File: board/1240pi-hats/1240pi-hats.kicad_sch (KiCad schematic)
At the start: 0 parts

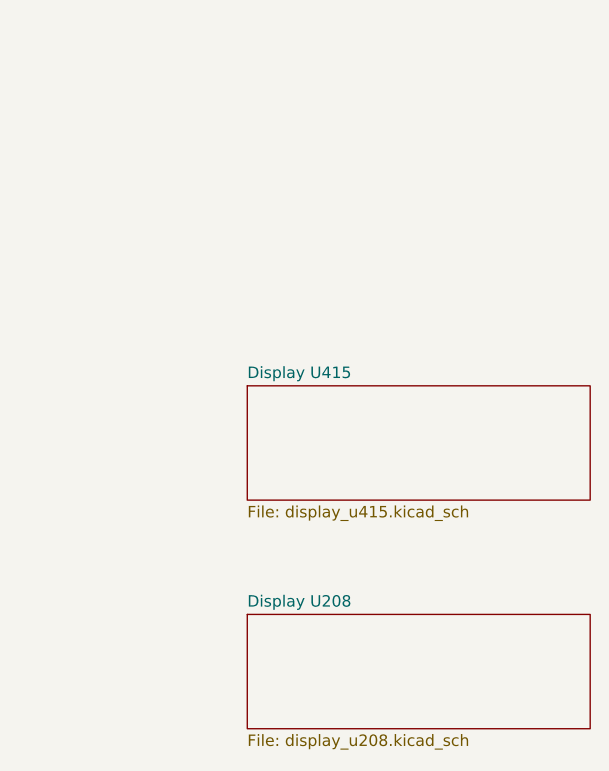
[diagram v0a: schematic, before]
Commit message: Redesign display hat to use a single board.
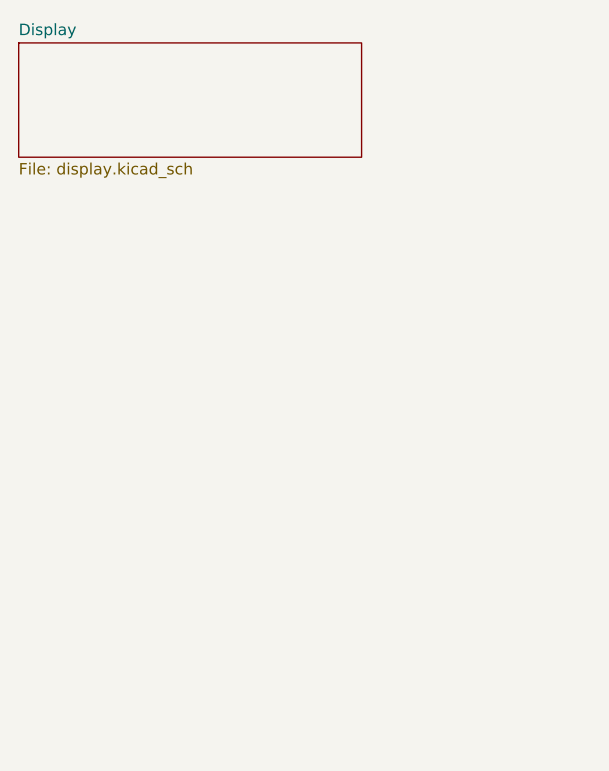
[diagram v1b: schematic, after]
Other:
- removed sheet Display U208
- removed sheet Display U415
- added sheet Display (display.kicad_sch)
- title: (none) -> 1240-Pi Mod Hats

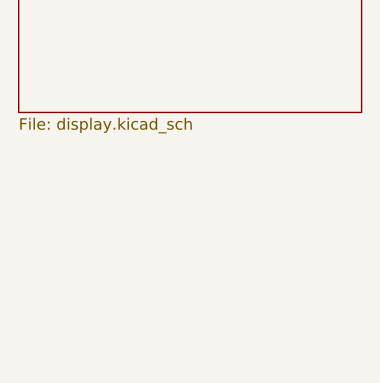
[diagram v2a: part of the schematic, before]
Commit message: Add IO Processor hat board.
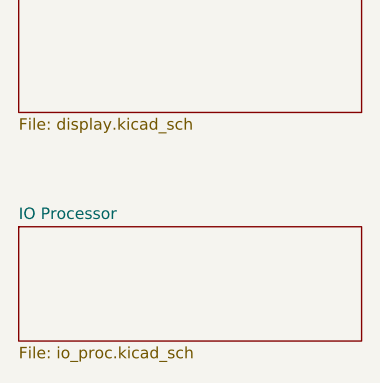
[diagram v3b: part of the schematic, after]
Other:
- added sheet IO Processor (io_proc.kicad_sch)
- company: (none) -> © 2022 Sam Hanes, licensed under CERN-OHL-P v2
- title: 1240-Pi Mod Hats -> 1240-Pi Modification Boards
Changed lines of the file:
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@@
   (paper "USLetter")
   (title_block
-    (title "1240-Pi Mod Hats")
-    (date "2022-04-20")
+    (title "1240-Pi Modification Boards")
+    (date "2022-04-21")
     (rev "1.0")
+    (company "© 2022 Sam Hanes, licensed under CERN-OHL-P v2")
+    (comment 1 "https://github.com/Elemecca/1240pi")
   )
   (sheet (at 38.1 38.1) (size 38.1 12.7) (fields_autoplaced)
@@
     )
   )
+  (sheet (at 38.1 63.5) (size 38.1 12.7) (fields_autoplaced)
+    (stroke (width 0.1524) (type solid) (color 0 0 0 0))
+    (fill (color 0 0 0 0.0000))
+    (property "Sheet name" "IO Processor" (id 0) (at 38.1 62.7884 0)
+      (effects (font (size 1.27 1.27)) (justify left bottom))
+    )
+    (property "Sheet file" "io_proc.kicad_sch" (id 1) (at 38.1 76.7846 0)
+      (effects (font (size 1.27 1.27)) (justify left top))
+    )
+  )
   (sheet_instances
     (path "/" (page "1"))
     (path "/600cca17-1832-4150-bdc4-60308bd69c4d" (page "2"))
+    (path "/93c3fd30-89aa-4f2c-a472-3cf6e18bbdfb" (page "3"))
   )
   (symbol_instances
@@
     (path "/600cca17-1832-4150-bdc4-60308bd69c4d/3702cd3c-879c-4c20-9276-eeaab458842a"
       (reference "#FLG0102") (unit 1) (value "PWR_FLAG") (footprint "")
+    )
+    (path "/93c3fd30-89aa-4f2c-a472-3cf6e18bbdfb/541631f1-5c6b-4984-b80b-da5d814ddc2a"
+      (reference "#FLG0103") (unit 1) (value "PWR_FLAG") (footprint "")
+    )
+    (path "/93c3fd30-89aa-4f2c-a472-3cf6e18bbdfb/b59ec72b-cbb3-4a84-b409-cb1a12e8909e"
+      (reference "#FLG0104") (unit 1) (value "PWR_FLAG") (footprint "")
     )
     (path "/600cca17-1832-4150-bdc4-60308bd69c4d/33dc1d17-3c43-484e-a994-57309880e165"
@@
     )
     (path "/600cca17-1832-4150-bdc4-60308bd69c4d/80a0843d-8e1d-4eab-9068-32674a47fe97"
-      (reference "#PWR?") (unit 1) (value "GND") (footprint "")
+      (reference "#PWR0105") (unit 1) (value "GND") (footprint "")
+    )
+    (path "/93c3fd30-89aa-4f2c-a472-3cf6e18bbdfb/34c1fa01-b507-49e3-9b9f-c468b6e77596"
+      (reference "#PWR0106") (unit 1) (value "~") (footprint "")
+    )
+    (path "/93c3fd30-89aa-4f2c-a472-3cf6e18bbdfb/534827d0-458c-4104-bc6d-0255ad697b4c"
+      (reference "#PWR0107") (unit 1) (value "+5V") (footprint "")
+    )
+    (path "/93c3fd30-89aa-4f2c-a472-3cf6e18bbdfb/805d731d-4180-4b8e-bf12-b88ccec030b8"
+      (reference "#PWR0108") (unit 1) (value "+5V") (footprint "")
+    )
+    (path "/93c3fd30-89aa-4f2c-a472-3cf6e18bbdfb/57c4d56d-de84-4172-ae0f-4c05a32da8d4"
+      (reference "#PWR0109") (unit 1) (value "GND") (footprint "")
+    )
+    (path "/93c3fd30-89aa-4f2c-a472-3cf6e18bbdfb/53181a90-a010-4b72-99ae-37b5bd3dc882"
+      (reference "#PWR0110") (unit 1) (value "+5V") (footprint "")
+    )
+    (path "/93c3fd30-89aa-4f2c-a472-3cf6e18bbdfb/2aecf130-835d-43a0-a6c9-612e14e7a782"
+      (reference "#PWR0111") (unit 1) (value "GND") (footprint "")
     )
     (path "/600cca17-1832-4150-bdc4-60308bd69c4d/75a11c0c-9043-4723-93bf-97178f7d2b90"
       (reference "J1") (unit 1) (value "Conn_02x05_Odd_Even") (footprint "Connector_PinHeader_2.54mm:PinHeader_2x05_P2.54mm_Vertical")
+    )
+    (path "/93c3fd30-89aa-4f2c-a472-3cf6e18bbdfb/f05fcee9-4158-40f8-b265-71b19b598390"
+      (reference "J21") (unit 1) (value "Conn_02x16_Odd_Even") (footprint "Connector_PinHeader_2.54mm:PinHeader_2x16_P2.54mm_Vertical")
     )
     (path "/600cca17-1832-4150-bdc4-60308bd69c4d/fc642cd8-7c35-4e61-a3f8-93bdddadf08c"
@@
       (reference "P415") (unit 3) (value "Header") (footprint "Package_DIP:DIP-14_W7.62mm")
     )
+    (path "/93c3fd30-89aa-4f2c-a472-3cf6e18bbdfb/8ad53c83-e421-4c0e-b4e0-361c324d4d58"
+      (reference "P445") (unit 1) (value "Header") (footprint "Package_DIP:DIP-40_W15.24mm")
+    )
+    (path "/93c3fd30-89aa-4f2c-a472-3cf6e18bbdfb/6c1a4460-5fc9-4b10-afd6-ed10a018878d"
+      (reference "Q21") (unit 1) (value "Q_PMOS_SGD") (footprint "Package_TO_SOT_THT:TO-92_Wide")
+    )
     (path "/600cca17-1832-4150-bdc4-60308bd69c4d/b91e8f31-48aa-4060-962c-f4d34479a4e2"
       (reference "R1") (unit 1) (value "4k7") (footprint "Resistor_THT:R_Axial_DIN0207_L6.3mm_D2.5mm_P10.16mm_Horizontal")
+    )
+    (path "/93c3fd30-89aa-4f2c-a472-3cf6e18bbdfb/39bc262a-7fca-4f46-a771-f7dcdf7ac0b0"
+      (reference "R21") (unit 1) (value "10k") (footprint "Resistor_THT:R_Axial_DIN0207_L6.3mm_D2.5mm_P10.16mm_Horizontal")
+    )
+    (path "/93c3fd30-89aa-4f2c-a472-3cf6e18bbdfb/e1046c61-4f21-4849-8a9a-39f81b175891"
+      (reference "R22") (unit 1) (value "10k") (footprint "Resistor_THT:R_Axial_DIN0207_L6.3mm_D2.5mm_P10.16mm_Horizontal")
     )
     (path "/600cca17-1832-4150-bdc4-60308bd69c4d/e66d8f6f-aa8b-48d8-bb2b-bde00dc24d64"
@@
       (reference "U415") (unit 3) (value "74S74") (footprint "Package_DIP:DIP-14_W7.62mm")
     )
+    (path "/93c3fd30-89aa-4f2c-a472-3cf6e18bbdfb/3a29e5d6-689f-46d7-a623-bc932a7056da"
+      (reference "U445") (unit 1) (value "Z80") (footprint "Package_DIP:DIP-40_W15.24mm_Socket")
+    )
   )
